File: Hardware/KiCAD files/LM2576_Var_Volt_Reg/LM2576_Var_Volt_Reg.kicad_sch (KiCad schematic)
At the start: 13 parts, among them J1 Conn_01x03_Pin, U2 LM2576HVS-ADJ

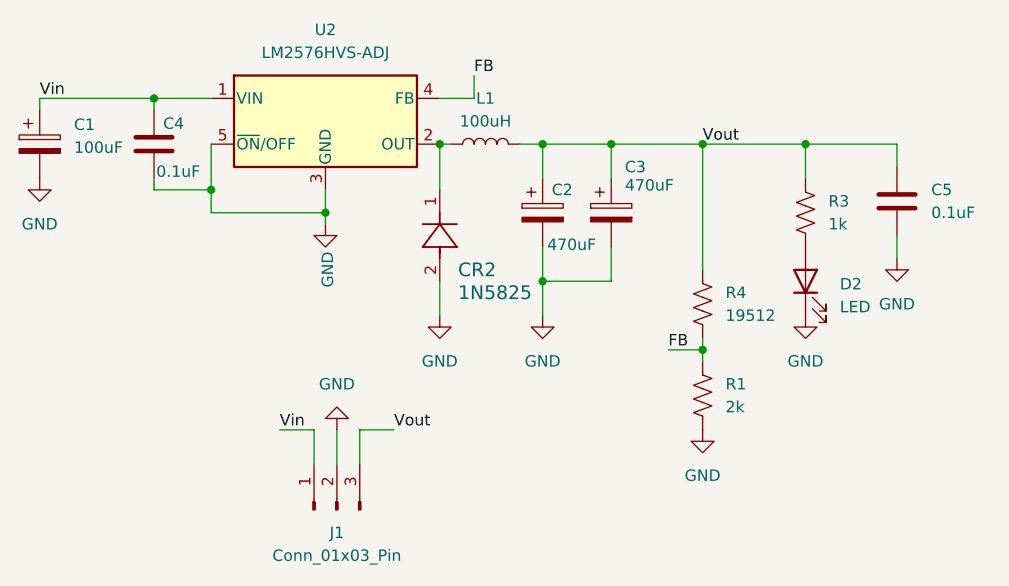
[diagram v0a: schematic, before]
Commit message: DRV 8825 and regulator purchased set
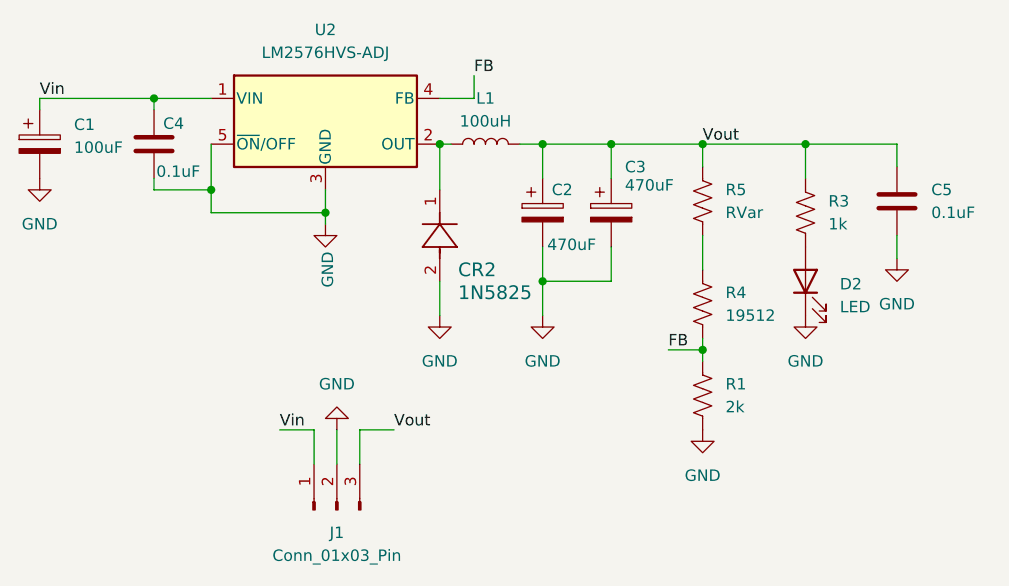
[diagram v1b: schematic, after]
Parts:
- added R5: RVar, Resistor_SMD:R_1206_3216Metric_Pad1.30x1.75mm_HandSolder, symbol Device:R_US
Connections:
- net Vout: now also R5.1; no longer R4.1
- new net: R4.1, R5.2
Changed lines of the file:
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@@
 	(paper "A4")
+	(junction
+		(at 162.56 85.09)
+		(diameter 0)
+		(color 0 0 0 0)
+	)
+	(junction
+		(at 107.95 67.31)
+		(diameter 0)
+		(color 0 0 0 0)
+	)
+	(junction
+		(at 144.78 62.23)
+		(diameter 0)
+		(color 0 0 0 0)
+	)
+	(junction
+		(at 173.99 62.23)
+		(diameter 0)
+		(color 0 0 0 0)
+	)
+	(junction
+		(at 120.65 69.85)
+		(diameter 0)
+		(color 0 0 0 0)
+	)
+	(junction
+		(at 144.78 77.47)
+		(diameter 0)
+		(color 0 0 0 0)
+	)
 	(junction
 		(at 162.56 62.23)
@@
 	)
 	(junction
-		(at 162.56 85.09)
-		(diameter 0)
-		(color 0 0 0 0)
-	)
-	(junction
-		(at 107.95 67.31)
-		(diameter 0)
-		(color 0 0 0 0)
-	)
-	(junction
-		(at 144.78 62.23)
-		(diameter 0)
-		(color 0 0 0 0)
-	)
-	(junction
-		(at 173.99 62.23)
-		(diameter 0)
-		(color 0 0 0 0)
-	)
-	(junction
-		(at 120.65 69.85)
-		(diameter 0)
-		(color 0 0 0 0)
-	)
-	(junction
-		(at 144.78 77.47)
-		(diameter 0)
-		(color 0 0 0 0)
-	)
-	(junction
 		(at 152.4 62.23)
 		(diameter 0)
@@
 	(wire
 		(pts
+			(xy 162.56 62.23) (xy 162.56 64.77)
+		)
+		(stroke
+			(width 0)
+			(type default)
+		)
+	)
+	(wire
+		(pts
 			(xy 101.6 57.15) (xy 101.6 58.42)
 		)
@@
 	(wire
 		(pts
-			(xy 162.56 62.23) (xy 162.56 76.2)
-		)
-		(stroke
-			(width 0)
-			(type default)
-		)
-	)
-	(wire
-		(pts
 			(xy 134.62 62.23) (xy 133.35 62.23)
 		)
@@
 	(wire
 		(pts
+			(xy 144.78 77.47) (xy 144.78 81.28)
+		)
+		(stroke
+			(width 0)
+			(type default)
+		)
+	)
+	(wire
+		(pts
+			(xy 173.99 62.23) (xy 184.15 62.23)
+		)
+		(stroke
+			(width 0)
+			(type default)
+		)
+	)
+	(wire
+		(pts
+			(xy 101.6 67.31) (xy 107.95 67.31)
+		)
+		(stroke
+			(width 0)
+			(type default)
+		)
+	)
+	(wire
+		(pts
+			(xy 133.35 62.23) (xy 133.35 67.31)
+		)
+		(stroke
+			(width 0)
+			(type default)
+		)
+	)
+	(wire
+		(pts
 			(xy 152.4 62.23) (xy 162.56 62.23)
 		)
@@
 	(wire
 		(pts
-			(xy 144.78 77.47) (xy 144.78 81.28)
-		)
-		(stroke
-			(width 0)
-			(type default)
-		)
-	)
-	(wire
-		(pts
-			(xy 173.99 62.23) (xy 184.15 62.23)
-		)
-		(stroke
-			(width 0)
-			(type default)
-		)
-	)
-	(wire
-		(pts
-			(xy 101.6 67.31) (xy 107.95 67.31)
-		)
-		(stroke
-			(width 0)
-			(type default)
-		)
-	)
-	(wire
-		(pts
-			(xy 133.35 62.23) (xy 133.35 67.31)
-		)
-		(stroke
-			(width 0)
-			(type default)
-		)
-	)
-	(wire
-		(pts
 			(xy 162.56 62.23) (xy 173.99 62.23)
 		)
@@
 		(pts
 			(xy 107.95 62.23) (xy 107.95 67.31)
+		)
+		(stroke
+			(width 0)
+			(type default)
+		)
+	)
+	(wire
+		(pts
+			(xy 162.56 72.39) (xy 162.56 76.2)
 		)
 		(stroke
@@
 					(unit 1)
 				)
+			)
+		)
+	)
+	(symbol
+		(lib_id "Device:R_US")
+		(at 162.56 68.58 0)
+		(unit 1)
+		(body_style 1)
+		(exclude_from_sim no)
+		(in_bom yes)
+		(on_board yes)
+		(in_pos_files yes)
+		(dnp no)
+		(fields_autoplaced yes)
+		(property "Reference" "R5"
+			(at 165.1 67.3099 0)
+			(show_name no)
+			(do_not_autoplace no)
+			(effects
+				(font
+					(size 1.27 1.27)
+				)
+				(justify left)
+			)
+		)
+		(property "Value" "RVar"
+			(at 165.1 69.8499 0)
+			(show_name no)
+			(do_not_autoplace no)
+			(effects
+				(font
+					(size 1.27 1.27)
+				)
+				(justify left)
+			)
+		)
+		(property "Footprint" "Resistor_SMD:R_1206_3216Metric_Pad1.30x1.75mm_HandSolder"
+			(at 163.576 68.834 90)
+			(hide yes)
+			(show_name no)
+			(do_not_autoplace no)
+			(effects
+				(font
+					(size 1.27 1.27)
+				)
+			)
+		)
+		(property "Datasheet" ""
+			(at 162.56 68.58 0)
+			(hide yes)
+			(show_name no)
+			(do_not_autoplace no)
+			(effects
+				(font
+					(size 1.27 1.27)
+				)
+			)
+		)
+		(property "Description" "Resistor, US symbol"
+			(at 162.56 68.58 0)
+			(hide yes)
+			(show_name no)
+			(do_not_autoplace no)
+			(effects
+				(font
+					(size 1.27 1.27)
+				)
+			)
+		)
+		(pin "1"
+		)
+		(pin "2"
+		)
+		(instances
+			(project "LM2576_Var_Volt_Reg"
+				(path "/05ad55a9-73a4-4419-8d6d-9b068d5aca56"
+					(reference "R5")
+					(unit 1)
+				)

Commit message: V1 boards after final board invoice
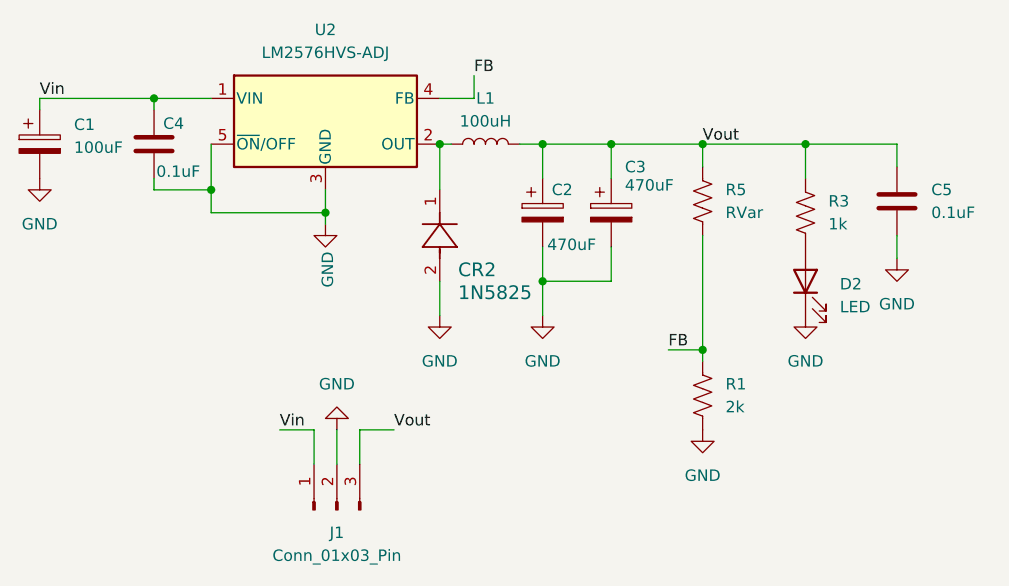
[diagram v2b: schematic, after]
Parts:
- removed R4: 19512, Resistor_SMD:R_1206_3216Metric_Pad1.30x1.75mm_HandSolder, symbol Device:R_US
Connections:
- net FB: now also R5.2
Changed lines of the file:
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@@
-	(wire
-		(pts
-			(xy 162.56 83.82) (xy 162.56 85.09)
-		)
-		(stroke
-			(width 0)
-			(type default)
-		)
-	)
 	(wire
 		(pts
@@
 	(wire
 		(pts
-			(xy 162.56 72.39) (xy 162.56 76.2)
+			(xy 162.56 72.39) (xy 162.56 85.09)
 		)
 		(stroke
@@
 					(unit 1)
 				)
-			)
-		)
-	)
-	(symbol
-		(lib_id "Device:R_US")
-		(at 162.56 80.01 0)
-		(unit 1)
-		(body_style 1)
-		(exclude_from_sim no)
-		(in_bom yes)
-		(on_board yes)
-		(in_pos_files yes)
-		(dnp no)
-		(fields_autoplaced yes)
-		(property "Reference" "R4"
-			(at 165.1 78.7399 0)
-			(show_name no)
-			(do_not_autoplace no)
-			(effects
-				(font
-					(size 1.27 1.27)
-				)
-				(justify left)
-			)
-		)
-		(property "Value" "19512"
-			(at 165.1 81.2799 0)
-			(show_name no)
-			(do_not_autoplace no)
-			(effects
-				(font
-					(size 1.27 1.27)
-				)
-				(justify left)
-			)
-		)
-		(property "Footprint" "Resistor_SMD:R_1206_3216Metric_Pad1.30x1.75mm_HandSolder"
-			(at 163.576 80.264 90)
-			(hide yes)
-			(show_name no)
-			(do_not_autoplace no)
-			(effects
-				(font
-					(size 1.27 1.27)
-				)
-			)
-		)
-		(property "Datasheet" ""
-			(at 162.56 80.01 0)
-			(hide yes)
-			(show_name no)
-			(do_not_autoplace no)
-			(effects
-				(font
-					(size 1.27 1.27)
-				)
-			)
-		)
-		(property "Description" "Resistor, US symbol"
-			(at 162.56 80.01 0)
-			(hide yes)
-			(show_name no)
-			(do_not_autoplace no)
-			(effects
-				(font
-					(size 1.27 1.27)
-				)
-			)
-		)
-		(pin "1"
-		)
-		(pin "2"
-		)
-		(instances
-			(project "LM2576_Var_Volt_Reg"
-				(path "/05ad55a9-73a4-4419-8d6d-9b068d5aca56"
-					(reference "R4")
-					(unit 1)
-				)

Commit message: V2 mainboard
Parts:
- R1: value 2k -> 1k
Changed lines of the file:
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@@
 			)
 		)
-		(property "Value" "2k"
+		(property "Value" "1k"
 			(at 165.1 91.4399 0)
 			(show_name no)
